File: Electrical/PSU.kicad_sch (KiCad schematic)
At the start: 120 parts, among them J15 Conn_01x03_Pin, J16 USB_C_Receptacle_USB2.0, Q10 2N7002, Q11 SSM3J332R,LF, Q12 SSM3J332R,LF, Q13 SSM3J332R,LF, Q14 SSM3J332R,LF, Q5 2N7002, Q6 2N7002, Q7 NCE30P28Q, Q8 2N7002, Q9 2N7002, SW1 SW_Push, U12 RP2040, U13 HT7533, U14 CH224Q_C46061833, U15 SY8253ADC, U16 SY8253ADC, U6 TL431DBZ, U7 SY8253ADC

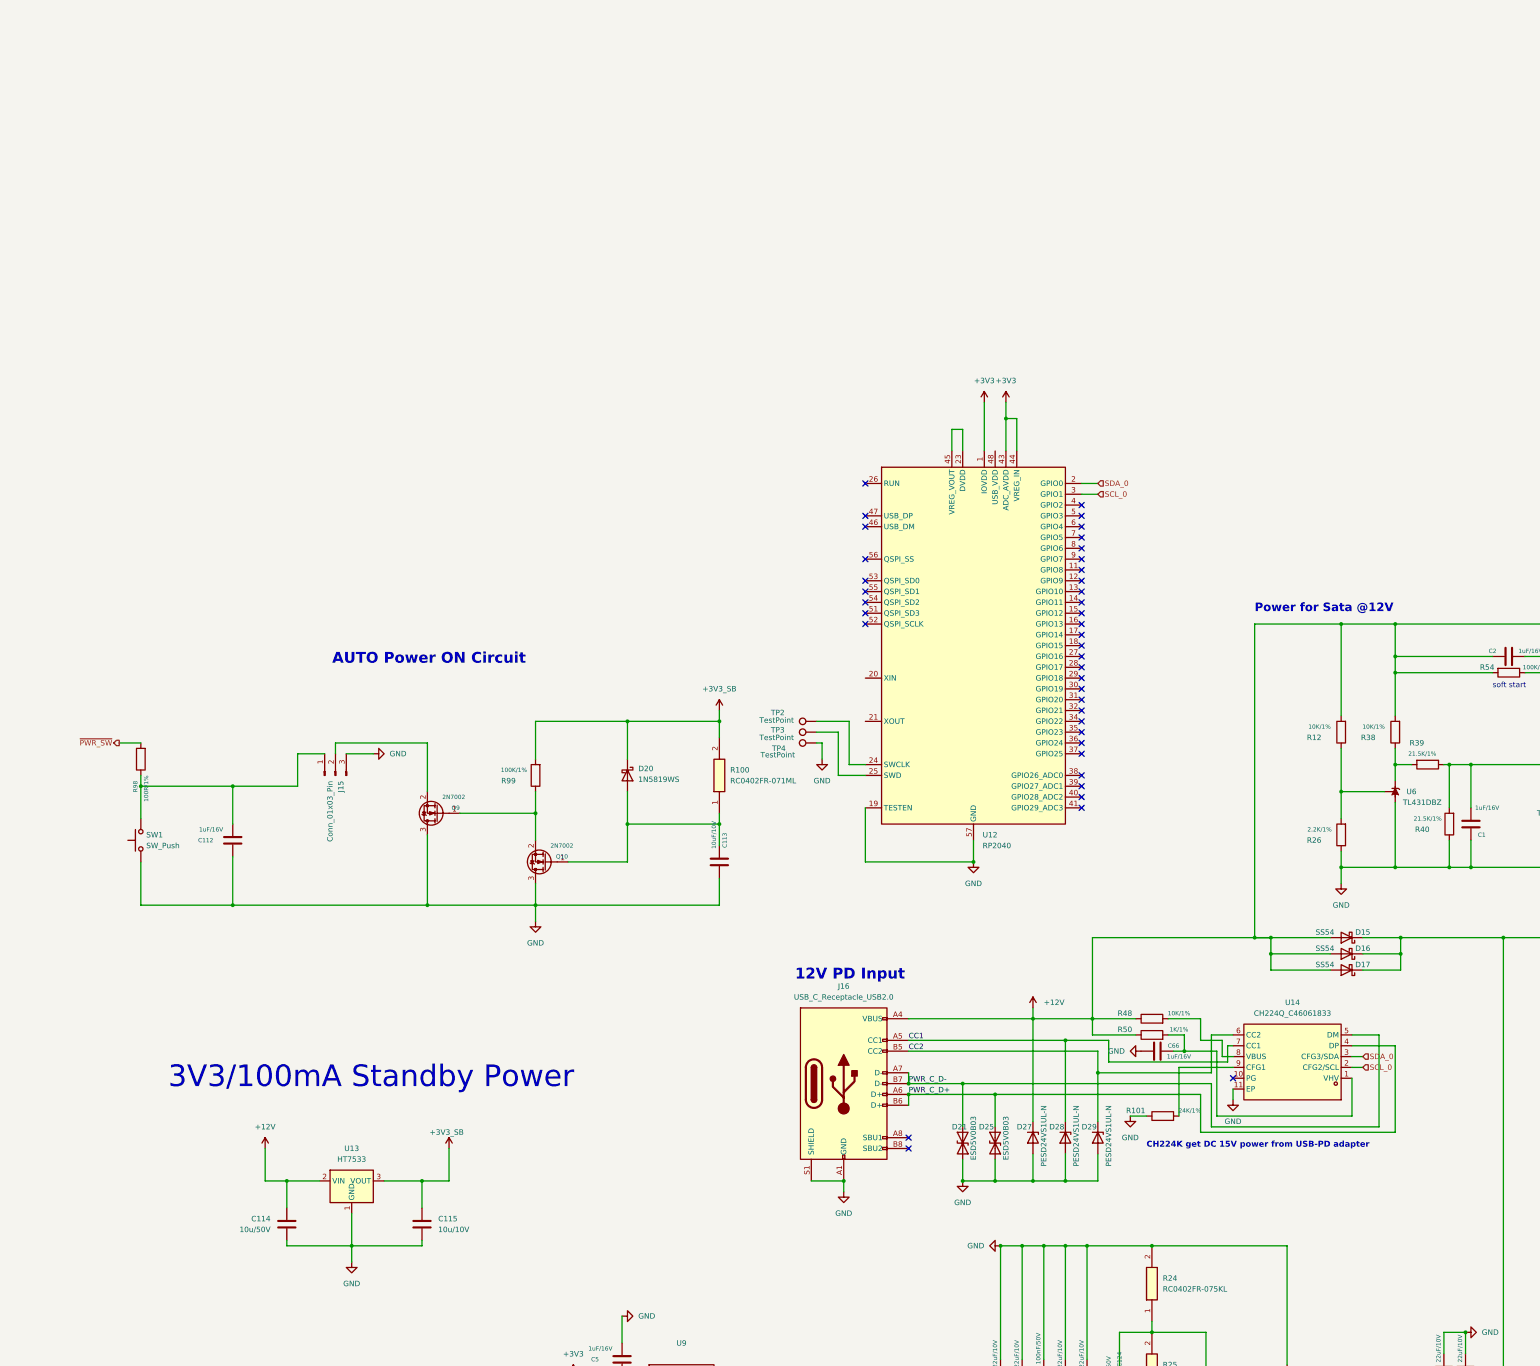
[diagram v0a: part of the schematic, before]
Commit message: add crystal for rp2040 and update readme
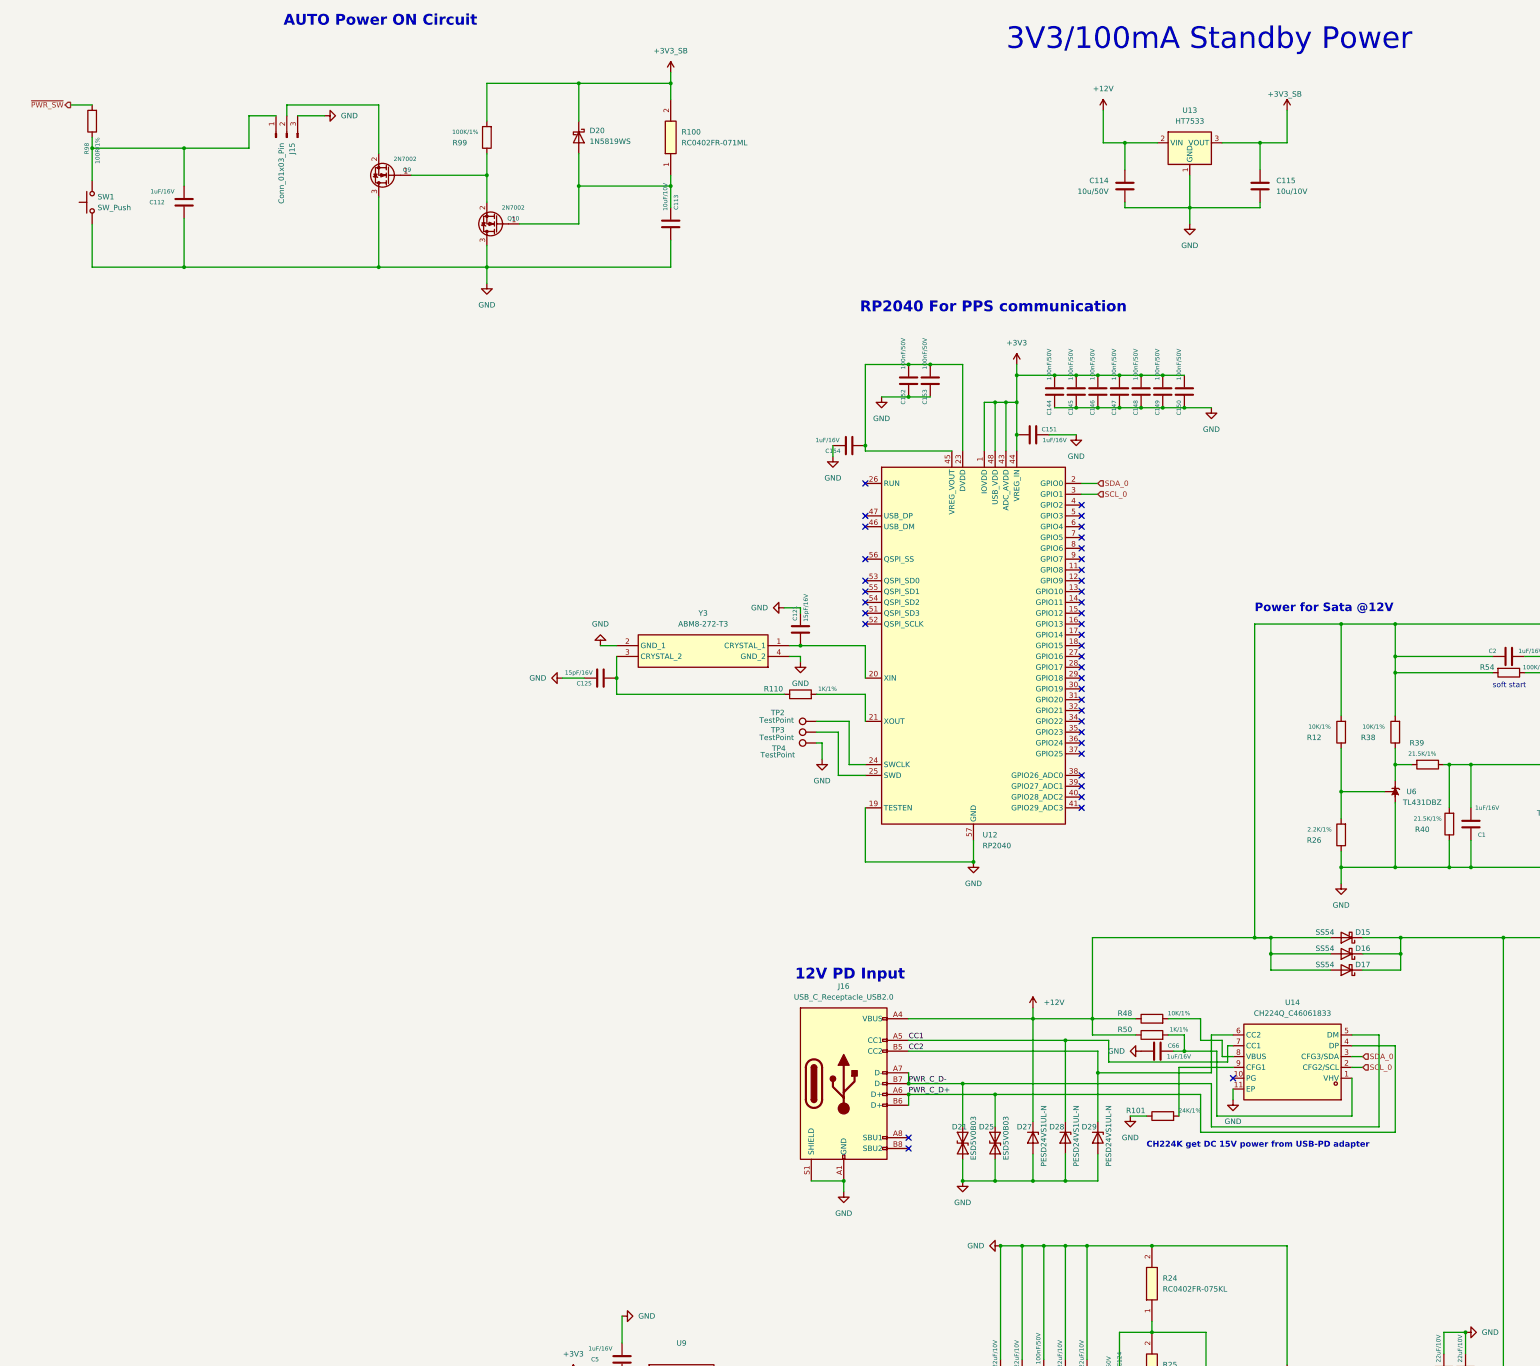
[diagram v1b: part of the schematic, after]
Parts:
- added C121, C125: 15pF/16V, A_HDJ_Library:C_0402_1005Metric, symbol Device:C
- added C144, C145, C146, C147, C148, C149, C150, C152, C153: 100nF/50V, A_HDJ_Library:C_0402_1005Metric, symbol Device:C
- added C151, C154: 1uF/16V, A_HDJ_Library:C_0402_1005Metric, symbol Device:C
- added R110: 1K/1%, A_HDJ_Library:R_0402_1005Metric, symbol Device:R
- added Y3: ABM8-272-T3, rp crystal:ABM8272T3, symbol rp crystal:ABM8-272-T3
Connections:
- net +3V3: now also U12.48 (USB_VDD), C144.2, C145.2, C146.2, C147.2, C148.2, C149.2, C150.2, C151.2
- net GND: now also C121.1, C125.1, C144.1, C145.1, C146.1, C147.1, C148.1, C149.1, C150.1, C151.1, C152.1, C153.1, C154.1, Y3.2 (GND_1), Y3.4 (GND_2)
- net at U12.20 (XIN): now also C121.2, Y3.1 (CRYSTAL_1)
- net at U12.21 (XOUT): now also R110.2
- net at U12.23 (DVDD), U12.45 (VREG_VOUT), U12.50 (DVDD): now also C152.2, C153.2, C154.2
- new net: C125.2, R110.1, Y3.3 (CRYSTAL_2)
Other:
- note added: "RP2040 For PPS communication"
- moved on the sheet: C112, C113, C114, C115, D20, J15, Q10, Q9, R100, R98, R99, SW1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

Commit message: switch to 20V PD input
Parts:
- removed C151, C154: 1uF/16V, A_HDJ_Library:C_0402_1005Metric, symbol Device:C
- removed C152, C153: 100nF/50V, A_HDJ_Library:C_0402_1005Metric, symbol Device:C
- removed TP2, TP3, TP4: TestPoint, A_HDJ_Library:TestPoint_Pad_D1.5mm, symbol Connector:TestPoint
- removed U12: RP2040, Package_DFN_QFN:QFN-56-1EP_7x7mm_P0.4mm_EP3.2x3.2mm, symbol MCU_RaspberryPi:RP2040
- removed Y3: ABM8-272-T3, rp crystal:ABM8272T3, symbol rp crystal:ABM8-272-T3
- added L3: 2.2uH/4.3A, A_HDJ_Library:L_Sunlord_SWPA4020S, symbol Device:L
- added R111: 10K/1%, A_HDJ_Library:R_0402_1005Metric, symbol Device:R
- added U12: SY8253ADC, Package_TO_SOT_SMD:TSOT-23-6, symbol Regulator_Switching:LM2734X
- C121: value 15pF/16V -> 100nF/50V
- C125: value 15pF/16V -> 12pF/50V; footprint A_HDJ_Library:C_0402_1005Metric -> Capacitor_SMD:C_0402_1005Metric
- C144, C145, C147, C148: value 100nF/50V -> 22uF/10V; footprint A_HDJ_Library:C_0402_1005Metric -> A_HDJ_Library:C_0603_1608Metric; SCH_Show_Footprint C0402 -> C603
- C149: value 100nF/50V -> 10uF/60V; footprint A_HDJ_Library:C_0402_1005Metric -> A_HDJ_Library:C_0603_1608Metric; SCH_Show_Footprint C0402 -> C603
- C150: value 100nF/50V -> 220nF/60V; footprint A_HDJ_Library:C_0402_1005Metric -> A_HDJ_Library:C_0603_1608Metric; SCH_Show_Footprint C0402 -> C603
- R101: value 24K/1% -> 120K/1%
- R110: value 1K/1% -> 191K/1%; footprint A_HDJ_Library:R_0402_1005Metric -> A_HDJ_Library:R_0603_1608Metric
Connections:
- net +12V: now also C125.1, C144.2, C145.2, C146.1, C147.2, C148.2, R110.2, L3.2; no longer C2.2, D15.2 (A), D16.2 (A), D17.2 (A), D27.1 (K), J16.A4 (VBUS), J16.A9 (VBUS), J16.B4 (VBUS), J16.B9 (VBUS), Q7.1 (S_1), Q7.10 (D_6), Q7.11 (D_7), Q7.2 (S_2), Q7.3 (S_3), Q7.5 (D_1), Q7.6 (D_2), Q7.7 (D_3), Q7.8 (D_4), Q7.9 (D_5), R12.2, R38.2, R48.1, R50.1, R54.2
- net +3V3: no longer C144.2, C145.2, C146.2, C147.2, C148.2, C149.2, C150.2
- net GND: now also C146.2, R111.1, U12.2 (GND); no longer C121.1, C125.1, C146.1
- net PWR_EN: now also U12.4 (EN)
- net at C125.2, R110.1: now also R111.2, U12.3 (FB)
- net at C121.2: now also U12.1 (BOOST)
- net SCL_0: no longer names the net of U14.2 (CFG2/SCL)
- net SDA_0: no longer names the net of U14.3 (CFG3/SDA)
- new net: C121.1, L3.1, U12.6 (SW)
- new net: C149.2, C150.2, Q7.10 (D_6), Q7.11 (D_7), Q7.5 (D_1), Q7.6 (D_2), Q7.7 (D_3), Q7.8 (D_4), Q7.9 (D_5), U12.5 (VIN)
- new net +20V: C2.2, D15.2 (A), D16.2 (A), D17.2 (A), D27.1 (K), J16.A4 (VBUS), J16.A9 (VBUS), J16.B4 (VBUS), J16.B9 (VBUS), Q7.1 (S_1), Q7.2 (S_2), Q7.3 (S_3), R12.2, R38.2, R48.1, R50.1, R54.2
- no-connect marks 40 -> 5
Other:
- note added: "20V PD Input"
- note added: "CH224Q get DC 28V power from USB-PD adapter"
- note removed: "12V PD Input"
- note removed: "CH224K get DC 15V power from USB-PD adapter"
- note removed: "RP2040 For PPS communication"
- moved on the sheet: C116, C117, C118, C119, Q11, Q12, Q13, Q14, R102, R103, R104, R105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
